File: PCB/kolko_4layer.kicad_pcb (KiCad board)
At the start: 4 copper layers, 141.4 x 141.4 mm, 85 parts, among them IC1 74HC4067PW-Q100J, J1 USB_C_Receptacle_USB2.0_16P, J2 Conn_01x02_Socket, J3 Conn_01x04_Socket, M2 MountingHole_2.2mm_M2, SW1 RST, SW2 BOOT, U1 ESP32-S3-WROOM-1, U2 USBLC6-2SC6, U3 AMS1117-3.3

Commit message: microphones routing imporvments
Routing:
- net /WSB: track 145.0 -> 156.3 mm
- net /DATAA: track 252.3 -> 258.6 mm
- net /WSA: track 244.6 -> 249.3 mm
- net /BCLKA: track 235.5 -> 238.3 mm
- net /BCLKB: track 161.0 -> 163.7 mm
- net /DATAB: track 157.1 -> 155.0 mm
- net +3.3V: track 912.8 -> 911.9 mm
- net /D_1MCU+: track 67.9 -> 67.2 mm
- net GND: track 87.7 -> 87.0 mm, vias 130 -> 120
- net /D_1MCU-: track 68.0 -> 67.3 mm
- net /ENS/RST: track 53.6 -> 54.2 mm
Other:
- board text added: "rev 1.0 10.2026 FFT Circle"
- board text removed: "Igor Oleksiewicz"

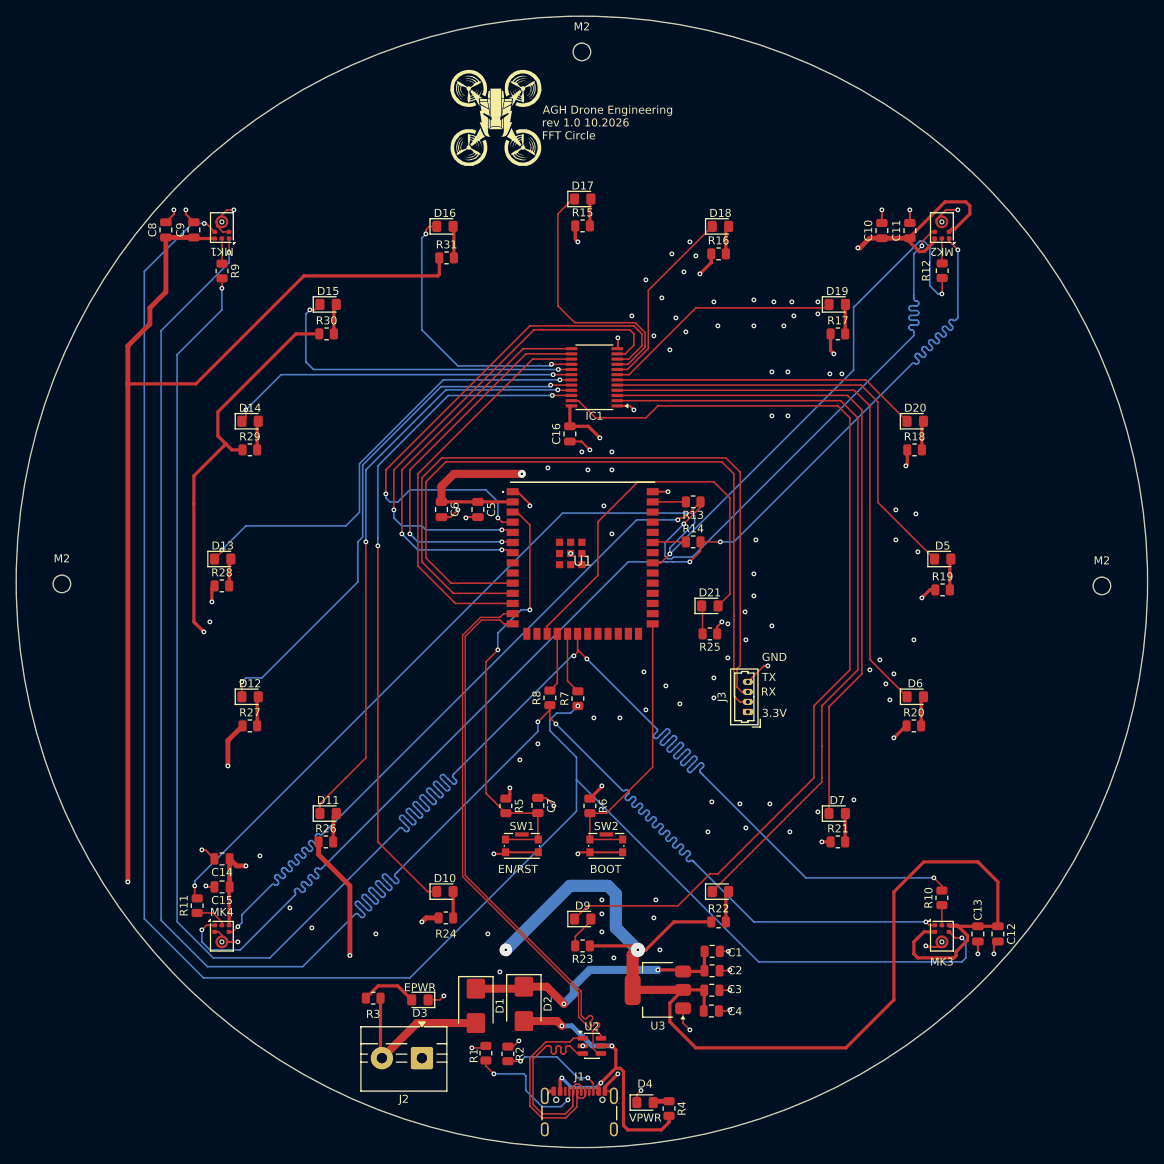
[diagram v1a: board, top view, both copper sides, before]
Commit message: add vias
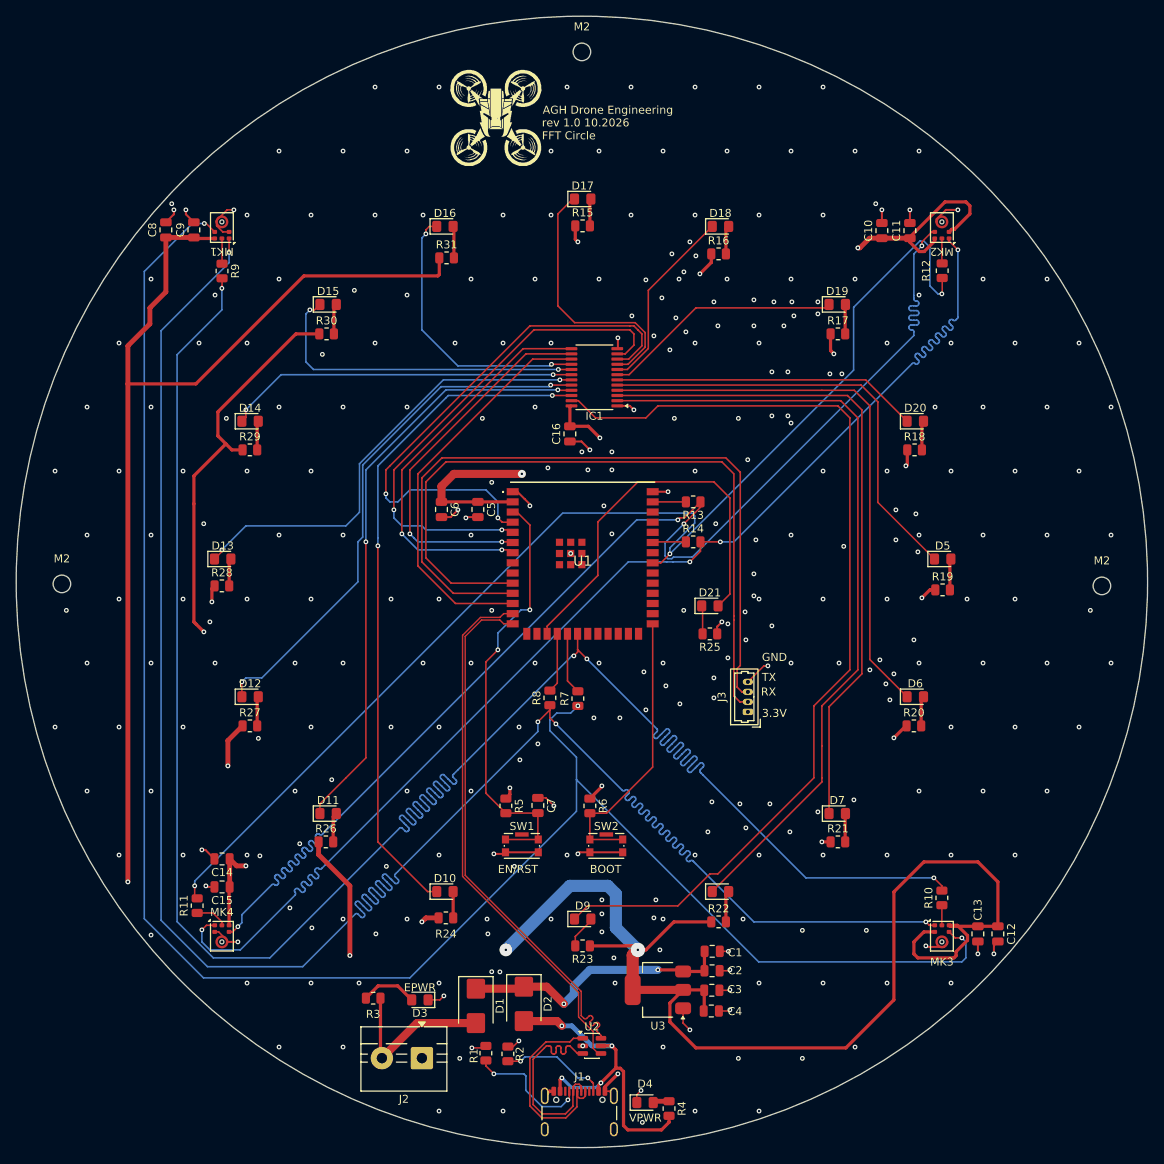
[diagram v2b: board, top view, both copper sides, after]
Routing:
- net GND: vias 120 -> 315

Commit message: final touches
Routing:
- net GND: vias 315 -> 312
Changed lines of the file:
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@@
-	)
-	(via
-		(at 171.25 77.75)
-		(size 0.6)
-		(drill 0.3)
-		(layers "F.Cu" "B.Cu")
-		(free yes)
-		(net 60)
 	)
 	(via
@@
 	)
 	(via
-		(at 133.75 142.5)
-		(size 0.6)
-		(drill 0.3)
-		(layers "F.Cu" "B.Cu")
-		(free yes)
-		(net 60)
-	)
-	(via
 		(at 163.644793 44.644793)
 		(size 0.6)
@@
 		(size 0.6)
 		(drill 0.3)
-		(layers "F.Cu" "B.Cu")
-		(free yes)
-		(net 60)
-	)
-	(via
-		(at 135.25 147.25)
-		(size 0.6)
-		(drill 0.3)
